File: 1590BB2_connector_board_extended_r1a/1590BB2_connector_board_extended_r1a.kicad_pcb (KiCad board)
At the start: 2 copper layers, 71.1 x 26.7 mm, 17 parts, among them J1 J1, J2 J2, J3 J3, J4 J4, X1 +, X2 -

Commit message: Minor changes
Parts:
- C3: footprint KCL:C-SM-1206 -> KCL-SM:C-SM-1206
- R1: footprint KCL:R-SM-1206 -> KCL-SM:R-SM-1206

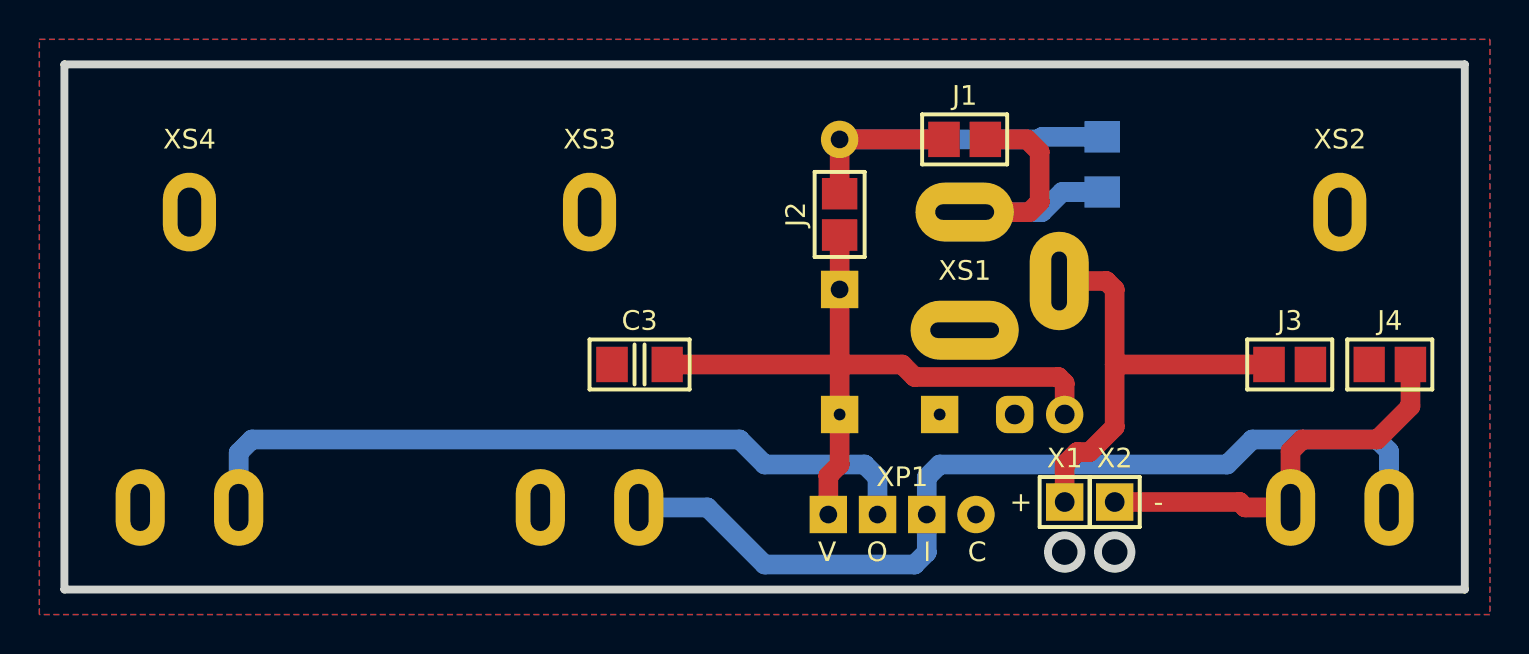
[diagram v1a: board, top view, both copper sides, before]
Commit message: 1590BB2 Connector Board Extended [REV1A]: buffer circuit added
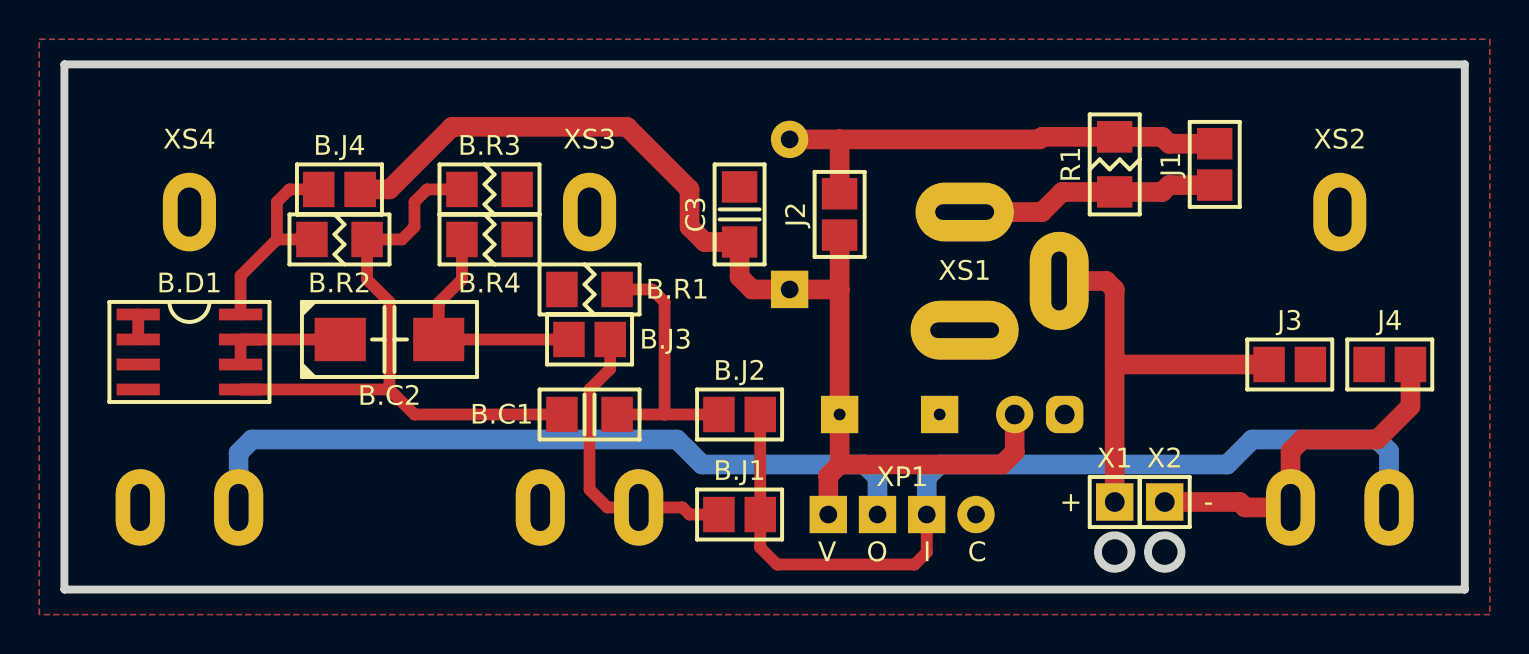
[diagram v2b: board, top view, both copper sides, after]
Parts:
- added B.C1: 105, KCL-SM:C-SM-1206, F.Cu at (96.5, 153.0)
- added B.C2: 106, KCL-SM:CP-CTSMD-C, F.Cu at (86.4, 149.2)
- added B.D1: 4558, KCL-SM:P-SO-08, F.Cu at (76.2, 149.9)
- added B.J1: B.J1, KCL:J-SB-1206-2, F.Cu at (104.1, 158.1)
- added B.J2: B.J2, KCL:J-SB-1206-2, F.Cu at (104.1, 153.0)
- added B.J3: B.J3, KCL:J-SB-1206-2, F.Cu at (96.5, 149.2)
- added B.J4: B.J4, KCL:J-SB-1206-2, F.Cu at (83.8, 141.6)
- added B.R1: 105, KCL-SM:R-SM-1206, F.Cu at (96.5, 146.7)
- added B.R2: 105, KCL-SM:R-SM-1206, F.Cu at (83.8, 144.1)
- added B.R3: 105, KCL-SM:R-SM-1206, F.Cu at (91.4, 141.6)
- added B.R4: 105, KCL-SM:R-SM-1206, F.Cu at (91.4, 144.1)
- R1: moved to F.Cu
- moved J1 12.8 mm to (128.3, 140.3), turned to 90 degrees
- moved C3 9.16 mm to (104.1, 142.9), turned to 90 degrees
- moved X2 2.54 mm to (125.7, 157.5)
- moved VD1 2.54 mm to (106.7, 142.9)
- moved X1 2.54 mm to (123.2, 157.5)
- moved R1 0.63 mm to (123.2, 140.3)
- turned C1 to 0 degrees
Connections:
- XS3 pad T: /IN-CON -> /DRY-OUT-CON
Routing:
- net Net-(B.C1-Pad2): track 0.00 -> 31.6 mm
- net V: track 36.6 -> 56.7 mm
- net /DRY-OUT-CON: track 0.00 -> 15.2 mm
- net /IN-BUF: track 0.00 -> 13.6 mm
- net /OUT-BUF: track 0.00 -> 12.2 mm
- net VBUF: track 0.00 -> 10.6 mm
- net Net-(B.C2-Pad+): track 0.00 -> 6.33 mm
- net Net-(J1-Pad1): track 17.0 -> 13.3 mm
- net Net-(J1-Pad2): track 21.4 -> 24.5 mm
- net /PP3-NEG: track 21.1 -> 18.5 mm
- net /PP3-POS: track 23.1 -> 21.6 mm
- net Net-(B.D1-Pad1): track 0.00 -> 1.27 mm
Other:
- outline, holes or cut-outs redrawn

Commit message: 1590BB2 Connector Board Extended [REV1A]: minor changes
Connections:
- net /IN-BUF renamed /BUF-IN
- net /OUT-BUF renamed /BUF-OUT

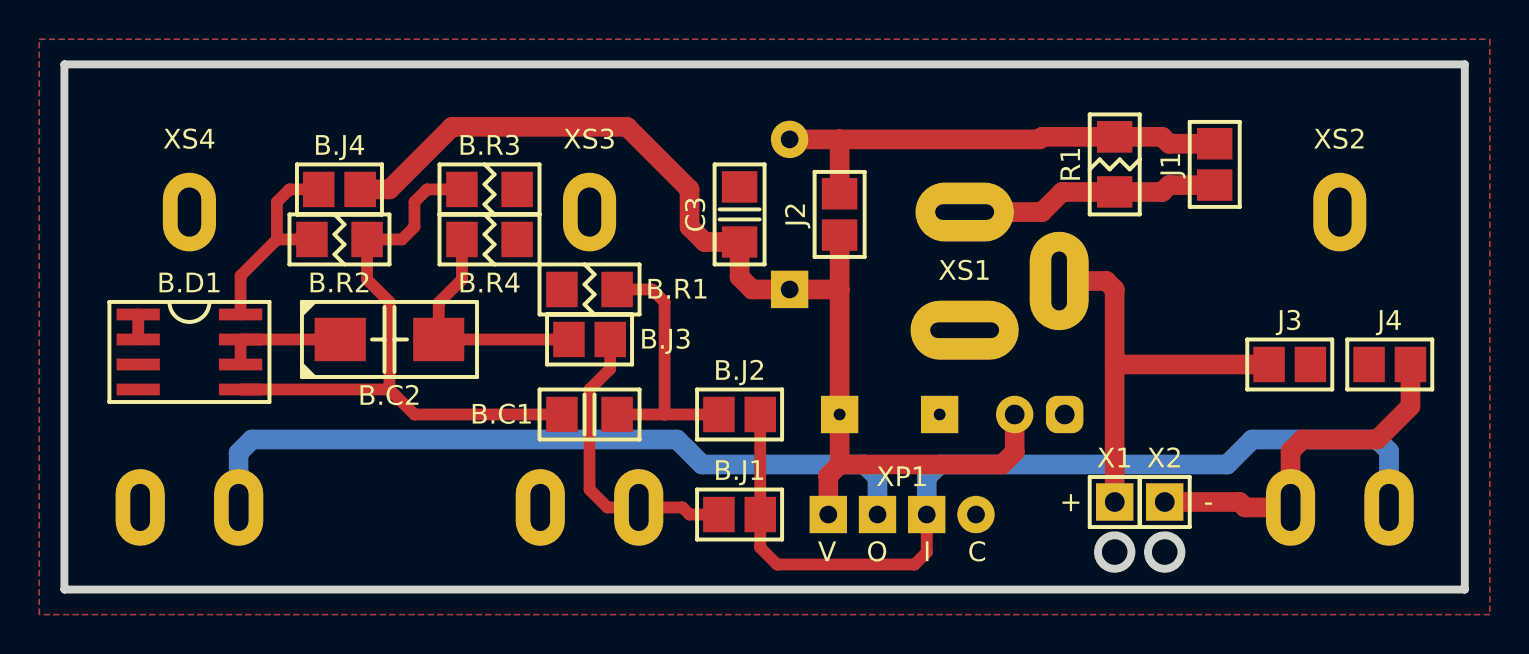
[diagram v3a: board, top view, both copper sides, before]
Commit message: 1590BB2 Connector Board Extended [REV1A]: toggle switch added, tantalum capacitor added
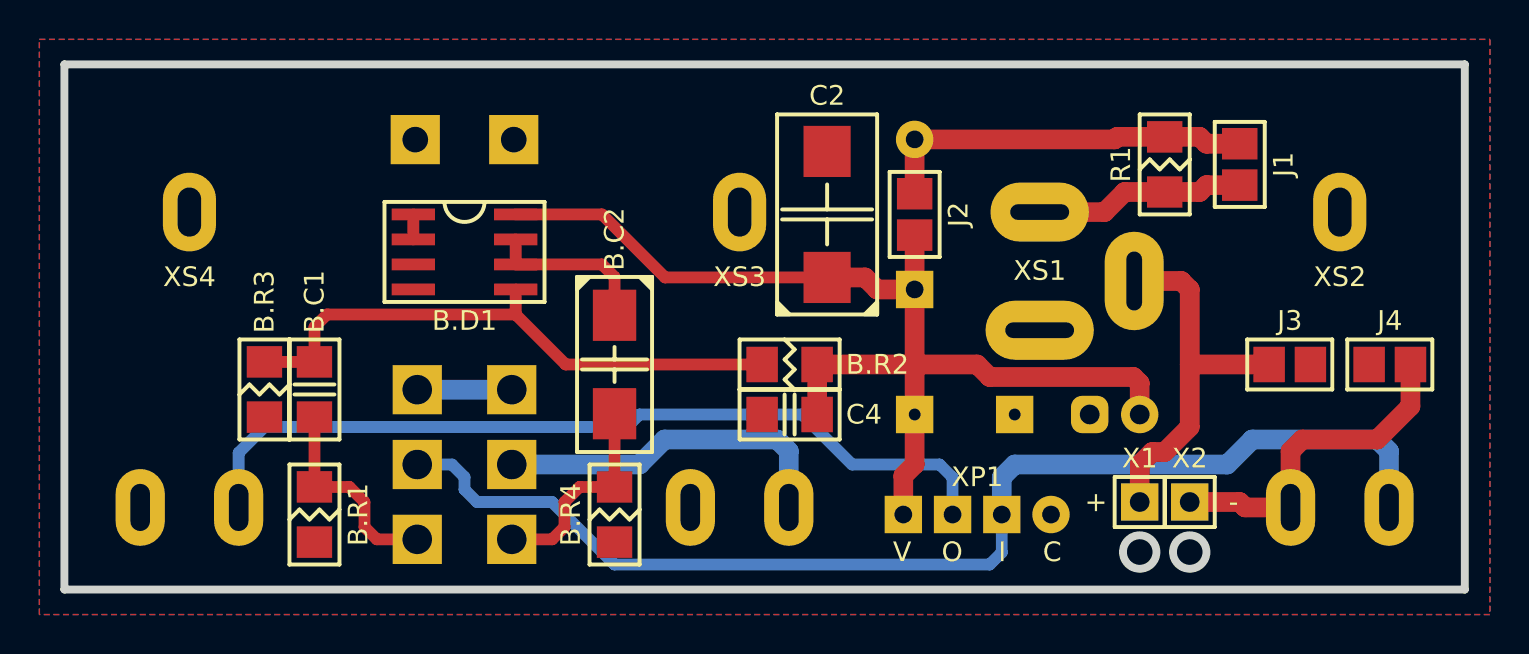
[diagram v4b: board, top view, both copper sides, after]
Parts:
- removed B.J1: B.J1, KCL:J-SB-1206-2
- removed B.J2: B.J2, KCL:J-SB-1206-2
- removed B.J3: B.J3, KCL:J-SB-1206-2
- removed B.J4: B.J4, KCL:J-SB-1206-2
- removed the C3 at (104.1, 142.9)
- added C2: 107, KCL-SM:CP-CTSMD-D, F.Cu at (108.6, 142.9)
- added C4: 104, KCL-SM:C-SM-1206, F.Cu at (106.7, 153.0)
- added SA1: MTS-202-C4, KCL-TH-ML:SW-MTS-202-C4-2.5, B.Cu at (90.2, 155.6)
- GB1: footprint KCL:B-PP3-HV -> KCL-VIRTUAL:B-PP3-HV
- moved B.R2 23.7 mm to (106.7, 150.5), turned to 0 degrees
- moved B.R1 18.1 mm to (82.5, 158.1), turned to 90 degrees
- moved B.R4 15.3 mm to (97.8, 158.1), turned to 90 degrees
- moved B.R3 15.3 mm to (80.0, 151.8), turned to 90 degrees
- moved B.D1 14.9 mm to (90.2, 144.8)
- moved B.C1 14.0 mm to (82.5, 151.8), turned to 90 degrees
- moved B.C2 11.5 mm to (97.8, 150.5), turned to 270 degrees
- moved XS3 7.62 mm to (104.1, 135.3)
- moved VD1 6.35 mm to (113.0, 142.9)
- moved C1 3.81 mm to (123.2, 153.0), turned to 180 degrees
- moved J2 3.81 mm to (113.0, 142.9)
- moved XP1 3.81 mm to (116.2, 158.1)
- moved XS1 3.81 mm to (119.4, 135.3)
- moved C3 3.81 mm to (115.6, 153.0)
- moved R1 2.54 mm to (125.7, 140.3)
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- renumbered C2 to C3
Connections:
- B.D1 pad 8: VBUF -> V
- B.R2 pad 2: VBUF -> V
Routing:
- net /IN-CON: track 47.0 -> 59.8 mm
- net VBUF: track 10.6 -> 0.00 mm
- net Net-(J1-Pad2): track 24.5 -> 19.5 mm
- net /OUT-CON: track 38.2 -> 43.0 mm
- net Net-(SA1-PadNO1): track 0.00 -> 4.80 mm
- net /BUF-IN: track 13.6 -> 10.6 mm
- net /DRY-OUT-CON: track 15.2 -> 17.7 mm
- net Net-(J1-Pad1): track 13.3 -> 10.7 mm
- net /PP3-POS: track 21.6 -> 19.2 mm
- net Net-(B.C2-Pad+): track 6.33 -> 8.50 mm
- net Net-(B.C1-Pad2): track 31.6 -> 29.6 mm
- net /BUF-OUT: track 12.2 -> 10.8 mm
- net /PP3-NEG: track 18.5 -> 17.2 mm
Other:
- outline, holes or cut-outs redrawn

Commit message: Minor changes
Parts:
- J1, J2, J3, J4: footprint KCL:J-SB-1206-2 -> KCL-SM:J-SB-1206-2
